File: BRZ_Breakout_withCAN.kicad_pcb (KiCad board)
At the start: 4 copper layers, 71.9 x 140.4 mm, 59 parts, among them J1 TC2030, J2 6376430-2, J3 6376430-2, J4 Conn_01x08_Socket, J5 Conn_01x08_Socket, J6 Conn_01x04_Socket, J7 Conn_01x10_Socket, Q1 NCV8402D, Q2 NCV8402D, U1 LD1117S33CTR, U2 MCP2562, U3 STM32F303K8T6, Y1 8MHz

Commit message: Fix the squiggles
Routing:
- net Net-(J2-Pad95): track 36.0 -> 39.0 mm
- net Net-(J2-Pad124): track 37.3 -> 38.6 mm
- net Net-(J2-Pad47): track 39.2 -> 40.1 mm
- net Net-(J2-Pad89): track 38.2 -> 39.1 mm
- net Net-(J2-Pad90): track 37.3 -> 38.2 mm
- net Net-(J2-Pad86): track 37.0 -> 37.8 mm
- net Net-(J2-Pad73): track 42.0 -> 41.3 mm
- net Net-(J2-Pad68): track 40.9 -> 40.2 mm
- net Net-(J2-Pad94): track 34.6 -> 35.3 mm
- net Net-(J2-Pad93): track 37.6 -> 38.3 mm
- net Net-(J2-Pad109): track 39.0 -> 39.6 mm
- net Net-(J2-Pad58): track 36.8 -> 37.4 mm
- net Net-(J2-Pad48): track 36.6 -> 37.2 mm
- net Net-(J2-Pad37): track 40.7 -> 40.2 mm
- net Net-(J2-Pad38): track 41.6 -> 41.1 mm
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- added copper zone on B.Cu, net +3V3
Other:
- board size 71.9 x 140.4 mm -> 71.9 x 142.4 mm

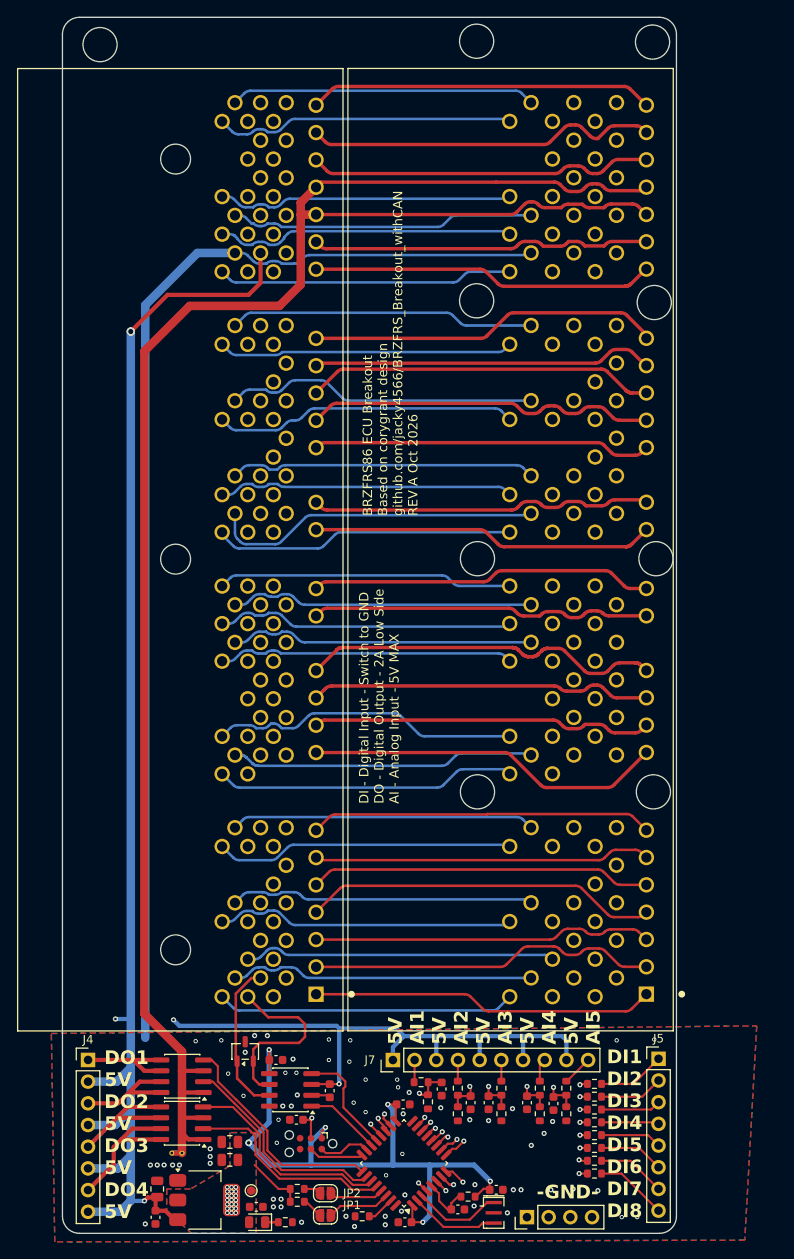
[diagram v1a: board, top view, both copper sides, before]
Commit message: Update Outline, Add breadboard area
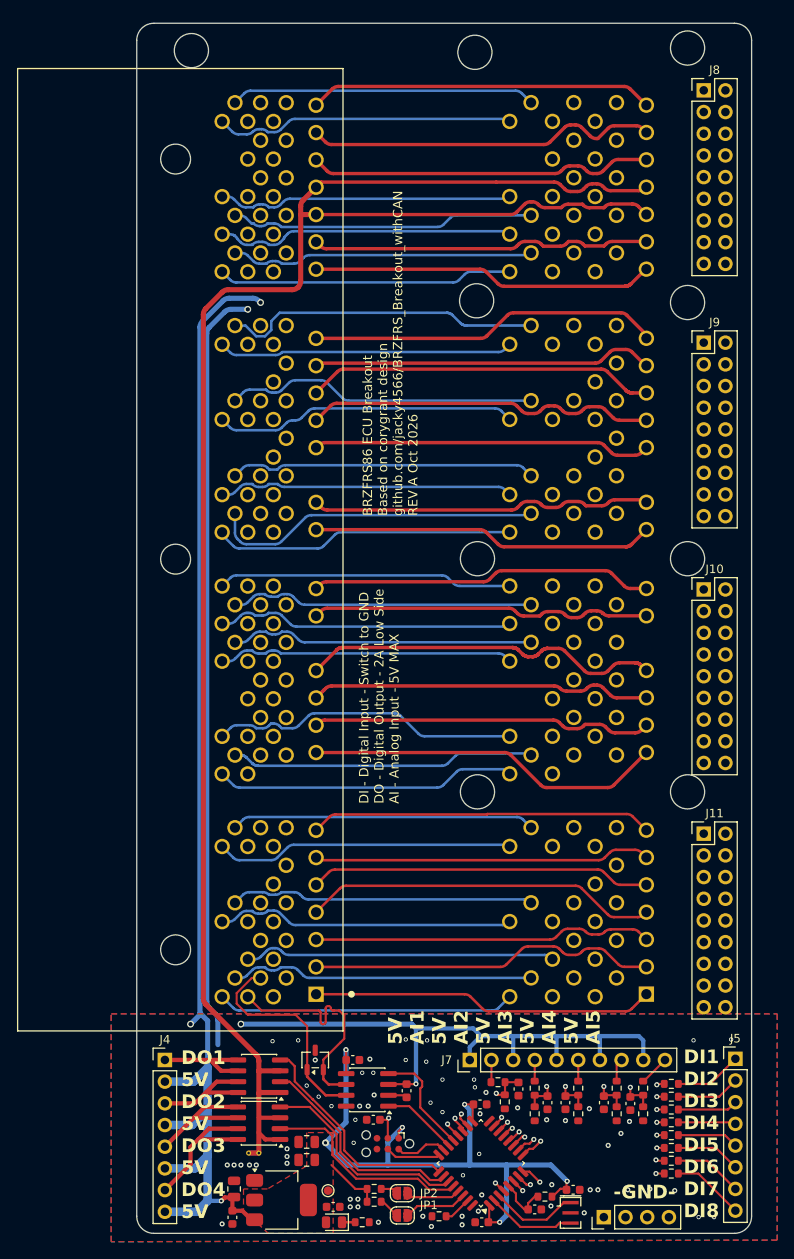
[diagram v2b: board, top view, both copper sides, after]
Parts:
- added J10: Conn_02x09_Counter_Clockwise, Connector_PinHeader_2.54mm:PinHeader_2x09_P2.54mm_Vertical, F.Cu at (146.4, 102.3)
- added J11: Conn_02x09_Counter_Clockwise, Connector_PinHeader_2.54mm:PinHeader_2x09_P2.54mm_Vertical, F.Cu at (146.4, 130.9)
- added J8: Conn_02x09_Counter_Clockwise, Connector_PinHeader_2.54mm:PinHeader_2x09_P2.54mm_Vertical, F.Cu at (146.4, 43.9)
- added J9: Conn_02x09_Counter_Clockwise, Connector_PinHeader_2.54mm:PinHeader_2x09_P2.54mm_Vertical, F.Cu at (146.4, 73.4)
- C1, C16, C2, C3, C4, C5, C6, C8, C9: value 100nF -> 0.1uF
- FB1: value ~ -> FERRITE BEAD 600 OHM 0603 1LN
- Q1, Q2: value NCV8402D -> NCV8402ADDR2G
- moved Y1 9.00 mm to (130.8, 175.3)
- moved C1 9.00 mm to (91.2, 175.8)
- moved C10 9.00 mm to (124.7, 160.8)
- moved C11 9.00 mm to (128.1, 162.4)
- moved C14 9.00 mm to (137.8, 162.5)
- moved C15 9.00 mm to (99.9, 169.1)
- moved C16 9.00 mm to (105.3, 157.4)
- moved C17 9.00 mm to (91.4, 172.5)
- moved C2 9.00 mm to (103.0, 174.6)
- moved C3 9.00 mm to (107.7, 164.4)
- moved C4 9.00 mm to (111.6, 161.0)
- moved C5 9.00 mm to (131.1, 172.6)
- moved C6 9.00 mm to (120.4, 176.4)
- moved C7 9.00 mm to (99.9, 167.0)
- moved C8 9.00 mm to (126.6, 174.9)
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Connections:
- net /12V_SW renamed Net-(J2-Pad1)
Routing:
- net /CAN_P: track 56.8 -> 64.0 mm
- net +5V: track 271.6 -> 265.8 mm
- net /CAN_N: track 58.8 -> 64.2 mm
- net GNDPWR: track 221.6 -> 218.0 mm
- net GND: track 136.9 -> 135.1 mm
- net Net-(J2-Pad101): track 35.8 -> 37.5 mm
- net +3V3: vias 27 -> 6
- removed copper zone on B.Cu, net +3V3
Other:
- board size 71.9 x 142.4 mm -> 72 x 141.7 mm
